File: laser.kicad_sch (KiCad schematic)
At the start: 15 parts, among them J3 Conn_Coaxial, Q1 BC547, Q2 BC547, U6 LM317_TO-220, U7 LM317_TO-220

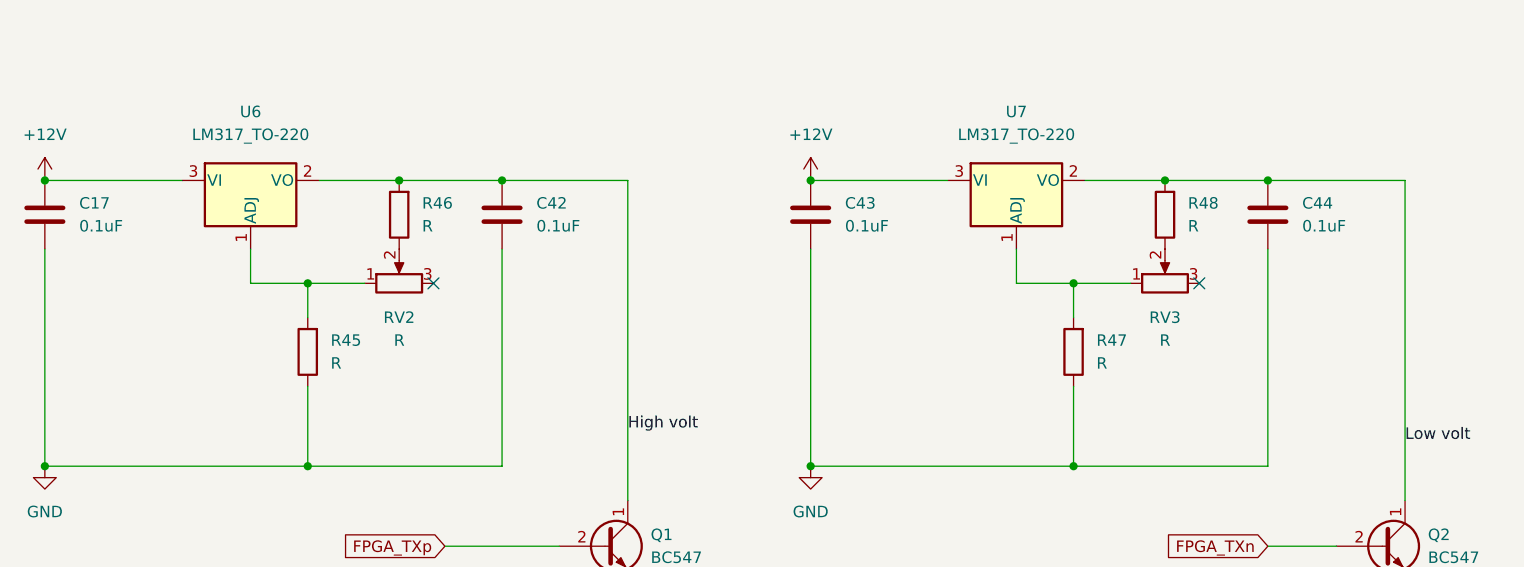
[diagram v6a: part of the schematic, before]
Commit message: added most of the sourcing info
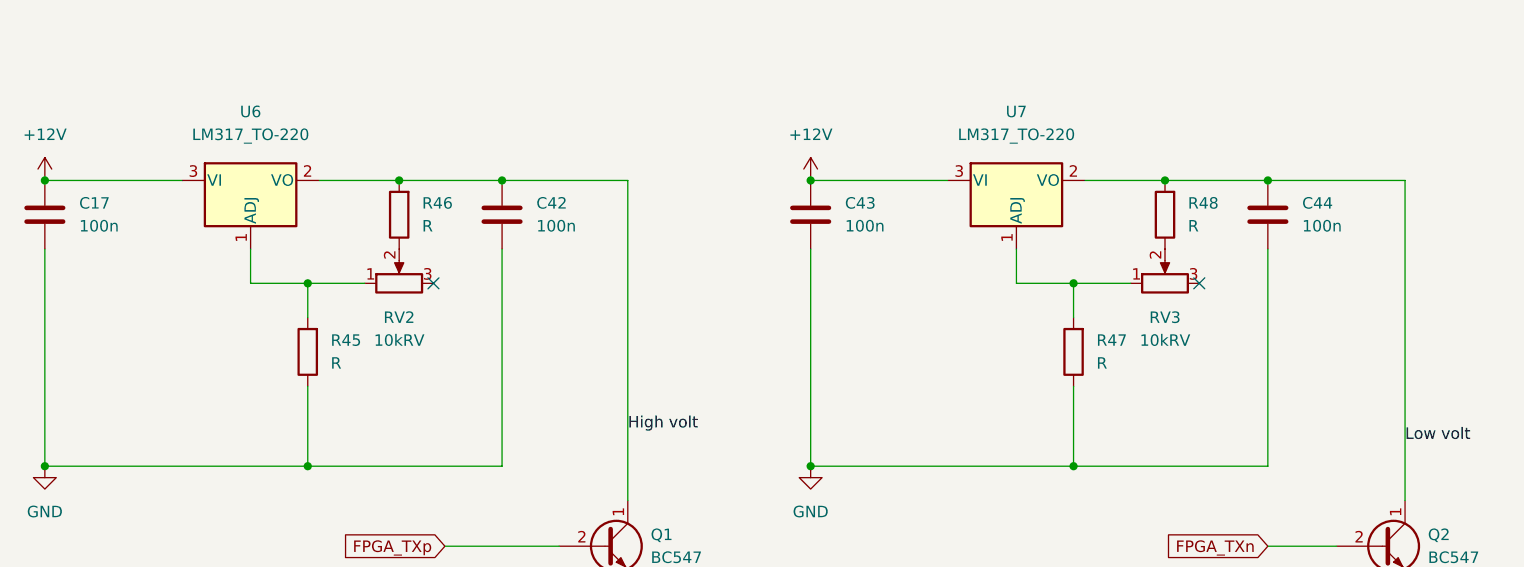
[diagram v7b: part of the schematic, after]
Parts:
- C17, C42, C43, C44: value 0.1uF -> 100n; Source (none) -> L3 store
- RV2, RV3: value R -> 10kRV; Source (none) -> https://onecall.farnell.com/vishay/t93yb104kt20/trimmer-pot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
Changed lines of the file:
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@@
       (effects (font (size 1.27 1.27)) (justify left))
     )
-    (property "Value" "0.1uF" (id 1) (at 180.34 52.0699 0)
+    (property "Value" "100n" (id 1) (at 180.34 52.0699 0)
       (effects (font (size 1.27 1.27)) (justify left))
     )
@@
     )
     (property "Datasheet" "~" (id 3) (at 176.53 50.8 0)
+      (effects (font (size 1.27 1.27)) hide)
+    )
+    (property "Source" "L3 store" (id 4) (at 176.53 50.8 0)
       (effects (font (size 1.27 1.27)) hide)
     )
@@
       (effects (font (size 1.27 1.27)) (justify left))
     )
-    (property "Value" "0.1uF" (id 1) (at 129.54 52.0699 0)
+    (property "Value" "100n" (id 1) (at 129.54 52.0699 0)
       (effects (font (size 1.27 1.27)) (justify left))
     )
@@
       (effects (font (size 1.27 1.27)) hide)
     )
+    (property "Source" "L3 store" (id 4) (at 125.73 50.8 0)
+      (effects (font (size 1.27 1.27)) hide)
+    )
     (pin "1")
     (pin "2")
@@
       (effects (font (size 1.27 1.27)) (justify left))
     )
-    (property "Value" "0.1uF" (id 1) (at 95.25 52.0699 0)
+    (property "Value" "100n" (id 1) (at 95.25 52.0699 0)
       (effects (font (size 1.27 1.27)) (justify left))
     )
@@
     )
     (property "Datasheet" "~" (id 3) (at 91.44 50.8 0)
+      (effects (font (size 1.27 1.27)) hide)
+    )
+    (property "Source" "L3 store" (id 4) (at 91.44 50.8 0)
       (effects (font (size 1.27 1.27)) hide)
     )
@@
     (in_bom yes) (on_board yes)
     (property "Reference" "RV2" (id 0) (at 80.01 62.23 90))
-    (property "Value" "R" (id 1) (at 80.01 64.77 90))
+    (property "Value" "10kRV" (id 1) (at 80.01 64.77 90))
     (property "Footprint" "Trimmer:T93YB104KT20" (id 2) (at 80.01 58.42 0)
       (effects (font (size 1.27 1.27)) hide)
@@
       (effects (font (size 1.27 1.27)) hide)
     )
+    (property "Source" "https://onecall.farnell.com/vishay/t93yb104kt20/trimmer-pot-100k-23turn-thd/dp/1141422" (id 4) (at 80.01 58.42 0)
+      (effects (font (size 1.27 1.27)) hide)
+    )
     (pin "1")
     (pin "2")
@@
       (effects (font (size 1.27 1.27)) (justify left))
     )
-    (property "Value" "0.1uF" (id 1) (at 44.45 52.0699 0)
+    (property "Value" "100n" (id 1) (at 44.45 52.0699 0)
       (effects (font (size 1.27 1.27)) (justify left))
     )
@@
     )
     (property "Datasheet" "~" (id 3) (at 40.64 50.8 0)
+      (effects (font (size 1.27 1.27)) hide)
+    )
+    (property "Source" "L3 store" (id 4) (at 40.64 50.8 0)
       (effects (font (size 1.27 1.27)) hide)
     )
@@
     (in_bom yes) (on_board yes)
     (property "Reference" "RV3" (id 0) (at 165.1 62.23 90))
-    (property "Value" "R" (id 1) (at 165.1 64.77 90))
+    (property "Value" "10kRV" (id 1) (at 165.1 64.77 90))
     (property "Footprint" "Trimmer:T93YB104KT20" (id 2) (at 165.1 58.42 0)
       (effects (font (size 1.27 1.27)) hide)
@@
       (effects (font (size 1.27 1.27)) hide)
     )
+    (property "Source" "https://onecall.farnell.com/vishay/t93yb104kt20/trimmer-pot-100k-23turn-thd/dp/1141422" (id 4) (at 165.1 58.42 0)
+      (effects (font (size 1.27 1.27)) hide)
+    )

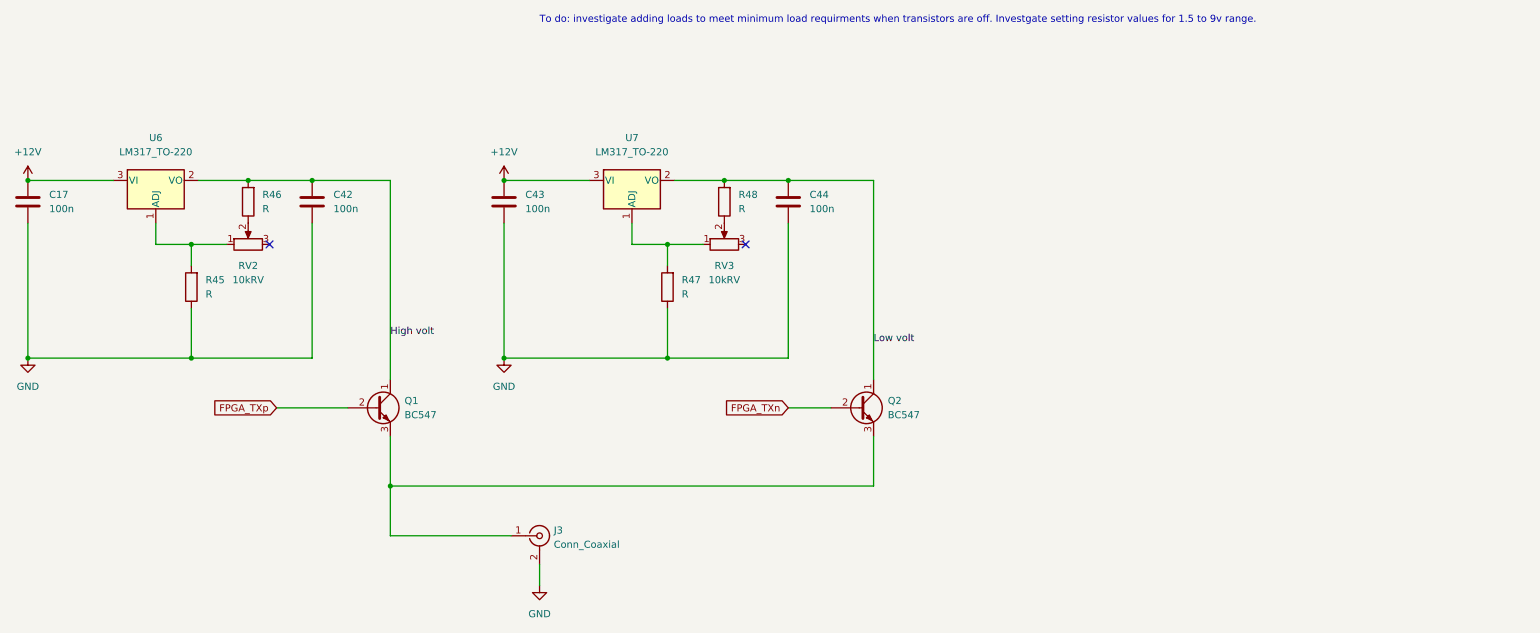
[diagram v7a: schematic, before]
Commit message: sorted power connectors, switching supply filtering, laser power
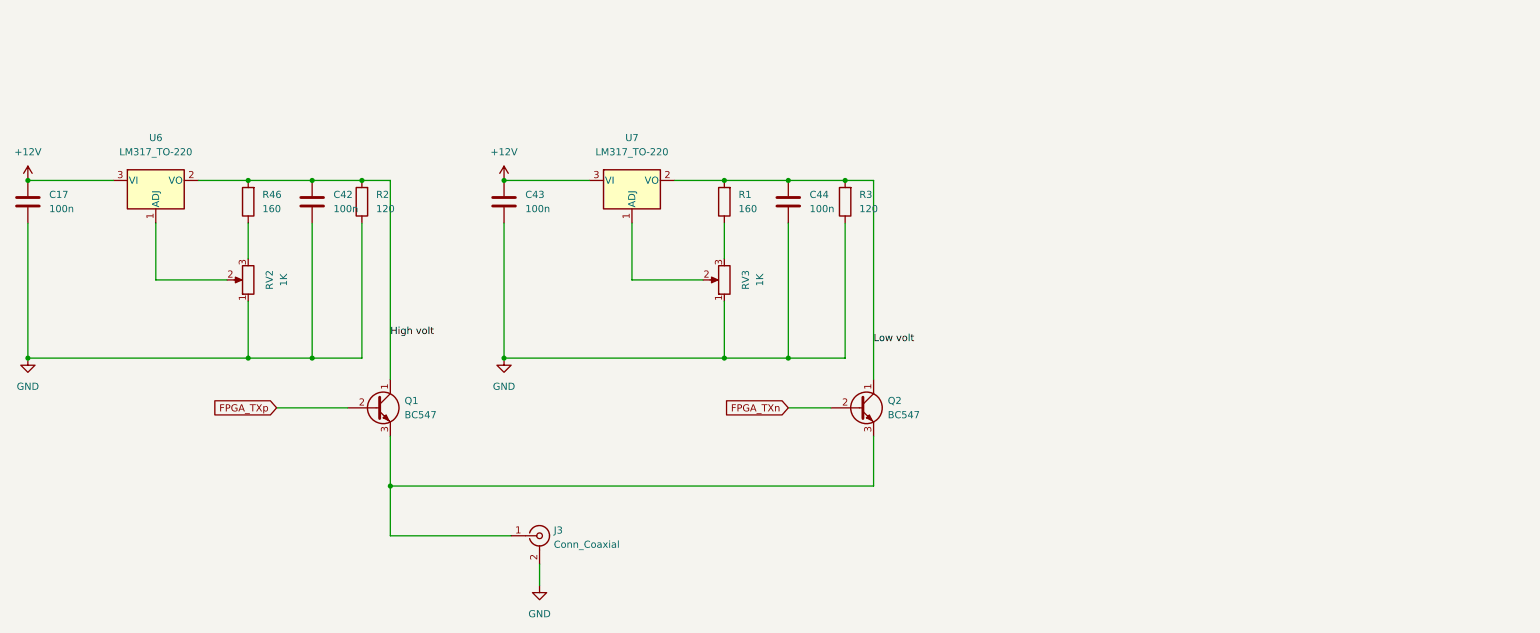
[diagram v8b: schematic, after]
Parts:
- removed R45, R47, R48: R, Resistor_SMD:R_0805_2012Metric_Pad1.20x1.40mm_HandSolder, symbol Device:R
- added R1: 160, Resistor_SMD:R_0805_2012Metric_Pad1.20x1.40mm_HandSolder, symbol Device:R
- added R2, R3: 120, Resistor_SMD:R_0805_2012Metric_Pad1.20x1.40mm_HandSolder, symbol Device:R
- R46: value R -> 160
- RV2, RV3: value 10kRV -> 1K
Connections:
- net GND: now also RV2.1, RV3.1, R2.1, R3.1
- net High volt: now also R2.2
- net Low volt: now also R1.2, R3.2
- net at U6.1 (ADJ): now also RV2.2; no longer RV2.1
- net at R46.1: now also RV2.3; no longer RV2.2
- net at RV3.2: now also U7.1 (ADJ)
- net at RV3.3: now also R1.1
- no-connect marks 2 -> 0
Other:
- note removed: "To do: investigate adding loads to meet minimum load requirments when transistors are off. Investgate setting resistor values for 1.5 to 9v range."
- moved on the sheet: RV2
